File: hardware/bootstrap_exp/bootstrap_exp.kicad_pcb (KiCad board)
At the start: 4 copper layers, 45.7 x 35.6 mm, 27 parts, among them J1 Conn_Coaxial, J2 Conn_Coaxial, U1 OPA810DBV, U2 OPA810DBV, U3 OPA810DBV

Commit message: Assign names to nets
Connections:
- net Net-(R2-Pad2) renamed /BOOT_DIV
- net Net-(R4-Pad2) renamed /BOOT
- net Net-(TP5-Pad1) renamed /FRONT_OUT
- net Net-(TP6-Pad1) renamed /BOOT_BUF
- net Net-(TP7-Pad1) renamed /AMP_OUT
- net Net-(U1-Pad3) renamed /FRONT_IN
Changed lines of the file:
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@@
   (net 3 "GND")
   (net 4 "/V-")
-  (net 5 "Net-(U1-Pad3)")
+  (net 5 "/FRONT_IN")
   (net 6 "Net-(J2-Pad1)")
-  (net 7 "Net-(TP5-Pad1)")
-  (net 8 "Net-(R2-Pad2)")
-  (net 9 "Net-(R4-Pad2)")
-  (net 10 "Net-(TP6-Pad1)")
-  (net 11 "Net-(TP7-Pad1)")
+  (net 7 "/FRONT_OUT")
+  (net 8 "/BOOT_DIV")
+  (net 9 "/BOOT")
+  (net 10 "/BOOT_BUF")
+  (net 11 "/AMP_OUT")
   (footprint "Resistor_SMD:R_0603_1608Metric" (layer "F.Cu")
     (at 132.1562 100.33)
@@
     (fp_line (start -0.8 -0.4125) (end 0.8 -0.4125) (layer "F.Fab") (width 0.1))
     (pad "1" smd roundrect (at -0.825 0) (size 0.8 0.95) (layers "F.Cu" "F.Paste" "F.Mask") (roundrect_rratio 0.25)
-      (net 8 "Net-(R2-Pad2)") (pintype "passive"))
+      (net 8 "/BOOT_DIV") (pintype "passive"))
     (pad "2" smd roundrect (at 0.825 0) (size 0.8 0.95) (layers "F.Cu" "F.Paste" "F.Mask") (roundrect_rratio 0.25)
       (net 3 "GND") (pintype "passive"))
@@
     (fp_line (start -0.8 -0.4125) (end 0.8 -0.4125) (layer "F.Fab") (width 0.1))
     (pad "1" smd roundrect (at -0.825 0) (size 0.8 0.95) (layers "F.Cu" "F.Paste" "F.Mask") (roundrect_rratio 0.25)
-      (net 9 "Net-(R4-Pad2)") (pintype "passive"))
+      (net 9 "/BOOT") (pintype "passive"))
     (pad "2" smd roundrect (at 0.825 0) (size 0.8 0.95) (layers "F.Cu" "F.Paste" "F.Mask") (roundrect_rratio 0.25)
-      (net 10 "Net-(TP6-Pad1)") (pintype "passive"))
+      (net 10 "/BOOT_BUF") (pintype "passive"))
     (model "${KICAD6_3DMODEL_DIR}/Resistor_SMD.3dshapes/R_0603_1608Metric.wrl"
       (offset (xyz 0 0 0))
@@
     (fp_line (start -0.8 1.45) (end -0.8 -1.05) (layer "F.Fab") (width 0.1))
     (pad "1" smd roundrect (at -1.1375 -0.95 180) (size 1.325 0.6) (layers "F.Cu" "F.Paste" "F.Mask") (roundrect_rratio 0.25)
-      (net 10 "Net-(TP6-Pad1)") (pintype "output"))
+      (net 10 "/BOOT_BUF") (pintype "output"))
     (pad "2" smd roundrect (at -1.1375 0 180) (size 1.325 0.6) (layers "F.Cu" "F.Paste" "F.Mask") (roundrect_rratio 0.25)
       (net 4 "/V-") (pinfunction "V-") (pintype "power_in"))
     (pad "3" smd roundrect (at -1.1375 0.95 180) (size 1.325 0.6) (layers "F.Cu" "F.Paste" "F.Mask") (roundrect_rratio 0.25)
-      (net 8 "Net-(R2-Pad2)") (pinfunction "+") (pintype "input"))
+      (net 8 "/BOOT_DIV") (pinfunction "+") (pintype "input"))
     (pad "4" smd roundrect (at 1.1375 0.95 180) (size 1.325 0.6) (layers "F.Cu" "F.Paste" "F.Mask") (roundrect_rratio 0.25)
-      (net 10 "Net-(TP6-Pad1)") (pinfunction "-") (pintype "input"))
+      (net 10 "/BOOT_BUF") (pinfunction "-") (pintype "input"))
     (pad "5" smd roundrect (at 1.1375 -0.95 180) (size 1.325 0.6) (layers "F.Cu" "F.Paste" "F.Mask") (roundrect_rratio 0.25)
       (net 2 "/V+") (pinfunction "V+") (pintype "power_in"))
@@
     (fp_circle (center 0 0) (end 1.6 0) (layer "F.Fab") (width 0.15) (fill none))
     (pad "1" thru_hole circle (at 0 0) (size 2.8 2.8) (drill 1.6) (layers *.Cu *.Mask)
-      (net 11 "Net-(TP7-Pad1)") (pinfunction "1") (pintype "passive"))
+      (net 11 "/AMP_OUT") (pinfunction "1") (pintype "passive"))
     (model "${KICAD6_3DMODEL_DIR}/TestPoint.3dshapes/TestPoint_Keystone_5005-5009_Compact.wrl"
       (offset (xyz 0 0 0))
@@
     (fp_line (start 0.8 0.4125) (end -0.8 0.4125) (layer "F.Fab") (width 0.1))
     (pad "1" smd roundrect (at -0.825 0 180) (size 0.8 0.95) (layers "F.Cu" "F.Paste" "F.Mask") (roundrect_rratio 0.25)
-      (net 7 "Net-(TP5-Pad1)") (pintype "passive"))
+      (net 7 "/FRONT_OUT") (pintype "passive"))
     (pad "2" smd roundrect (at 0.825 0 180) (size 0.8 0.95) (layers "F.Cu" "F.Paste" "F.Mask") (roundrect_rratio 0.25)
-      (net 8 "Net-(R2-Pad2)") (pintype "passive"))
+      (net 8 "/BOOT_DIV") (pintype "passive"))
     (model "${KICAD6_3DMODEL_DIR}/Resistor_SMD.3dshapes/R_0603_1608Metric.wrl"
       (offset (xyz 0 0 0))
@@
     (fp_circle (center 0 0) (end 1.6 0) (layer "F.Fab") (width 0.15) (fill none))
     (pad "1" thru_hole circle (at 0 0) (size 2.8 2.8) (drill 1.6) (layers *.Cu *.Mask)
-      (net 10 "Net-(TP6-Pad1)") (pinfunction "1") (pintype "passive"))
+      (net 10 "/BOOT_BUF") (pinfunction "1") (pintype "passive"))
     (model "${KICAD6_3DMODEL_DIR}/TestPoint.3dshapes/TestPoint_Keystone_5005-5009_Compact.wrl"
       (offset (xyz 0 0 0))
@@
     (fp_line (start -0.8 -0.4125) (end 0.8 -0.4125) (layer "F.Fab") (width 0.1))
     (pad "1" smd roundrect (at -0.825 0) (size 0.8 0.95) (layers "F.Cu" "F.Paste" "F.Mask") (roundrect_rratio 0.25)
-      (net 9 "Net-(R4-Pad2)") (pintype "passive"))
+      (net 9 "/BOOT") (pintype "passive"))
     (pad "2" smd roundrect (at 0.825 0) (size 0.8 0.95) (layers "F.Cu" "F.Paste" "F.Mask") (roundrect_rratio 0.25)
-      (net 8 "Net-(R2-Pad2)") (pintype "passive"))
+      (net 8 "/BOOT_DIV") (pintype "passive"))
     (model "${KICAD6_3DMODEL_DIR}/Resistor_SMD.3dshapes/R_0603_1608Metric.wrl"
       (offset (xyz 0 0 0))
@@
     (fp_line (start -0.8 0.4125) (end -0.8 -0.4125) (layer "F.Fab") (width 0.1))
     (pad "1" smd roundrect (at -0.825 0 270) (size 0.8 0.95) (layers "F.Cu" "F.Paste" "F.Mask") (roundrect_rratio 0.25)
-      (net 5 "Net-(U1-Pad3)") (pintype "passive"))
+      (net 5 "/FRONT_IN") (pintype "passive"))
     (pad "2" smd roundrect (at 0.825 0 270) (size 0.8 0.95) (layers "F.Cu" "F.Paste" "F.Mask") (roundrect_rratio 0.25)
-      (net 9 "Net-(R4-Pad2)") (pintype "passive"))
+      (net 9 "/BOOT") (pintype "passive"))
     (model "${KICAD6_3DMODEL_DIR}/Resistor_SMD.3dshapes/R_0603_1608Metric.wrl"
       (offset (xyz 0 0 0))
@@
     (fp_circle (center 0 0) (end 1.6 0) (layer "F.Fab") (width 0.15) (fill none))
     (pad "1" thru_hole circle (at 0 0) (size 2.8 2.8) (drill 1.6) (layers *.Cu *.Mask)
-      (net 7 "Net-(TP5-Pad1)") (pinfunction "1") (pintype "passive"))
+      (net 7 "/FRONT_OUT") (pinfunction "1") (pintype "passive"))
     (model "${KICAD6_3DMODEL_DIR}/TestPoint.3dshapes/TestPoint_Keystone_5005-5009_Compact.wrl"
       (offset (xyz 0 0 0))
@@
     (fp_line (start -0.8 -0.4) (end 0.8 -0.4) (layer "F.Fab") (width 0.1))
     (pad "1" smd roundrect (at -0.775 0 180) (size 0.9 0.95) (layers "F.Cu" "F.Paste" "F.Mask") (roundrect_rratio 0.25)
-      (net 5 "Net-(U1-Pad3)") (pintype "passive"))
+      (net 5 "/FRONT_IN") (pintype "passive"))
     (pad "2" smd roundrect (at 0.775 0 180) (size 0.9 0.95) (layers "F.Cu" "F.Paste" "F.Mask") (roundrect_rratio 0.25)
       (net 1 "Net-(C1-Pad2)") (pintype "passive"))
@@
     (fp_line (start 0.8 1.45) (end -0.8 1.45) (layer "F.Fab") (width 0.1))
     (pad "1" smd roundrect (at -1.1375 -0.95) (size 1.325 0.6) (layers "F.Cu" "F.Paste" "F.Mask") (roundrect_rratio 0.25)
-      (net 7 "Net-(TP5-Pad1)") (pintype "output"))
+      (net 7 "/FRONT_OUT") (pintype "output"))
     (pad "2" smd roundrect (at -1.1375 0) (size 1.325 0.6) (layers "F.Cu" "F.Paste" "F.Mask") (roundrect_rratio 0.25)
       (net 4 "/V-") (pinfunction "V-") (pintype "power_in"))
     (pad "3" smd roundrect (at -1.1375 0.95) (size 1.325 0.6) (layers "F.Cu" "F.Paste" "F.Mask") (roundrect_rratio 0.25)
-      (net 5 "Net-(U1-Pad3)") (pinfunction "+") (pintype "input"))
+      (net 5 "/FRONT_IN") (pinfunction "+") (pintype "input"))
     (pad "4" smd roundrect (at 1.1375 0.95) (size 1.325 0.6) (layers "F.Cu" "F.Paste" "F.Mask") (roundrect_rratio 0.25)
-      (net 7 "Net-(TP5-Pad1)") (pinfunction "-") (pintype "input"))
+      (net 7 "/FRONT_OUT") (pinfunction "-") (pintype "input"))
     (pad "5" smd roundrect (at 1.1375 -0.95) (size 1.325 0.6) (layers "F.Cu" "F.Paste" "F.Mask") (roundrect_rratio 0.25)
       (net 2 "/V+") (pinfunction "V+") (pintype "power_in"))
@@
     (fp_line (start 0.8 -0.4125) (end 0.8 0.4125) (layer "F.Fab") (width 0.1))
     (pad "1" smd roundrect (at -0.825 0) (size 0.8 0.95) (layers "F.Cu" "F.Paste" "F.Mask") (roundrect_rratio 0.25)
-      (net 11 "Net-(TP7-Pad1)") (pintype "passive"))
+      (net 11 "/AMP_OUT") (pintype "passive"))
     (pad "2" smd roundrect (at 0.825 0) (size 0.8 0.95) (layers "F.Cu" "F.Paste" "F.Mask") (roundrect_rratio 0.25)
       (net 6 "Net-(J2-Pad1)") (pintype "passive"))
@@
     (fp_line (start 0.8 -1.45) (end 0.8 1.45) (layer "F.Fab") (width 0.1))
     (pad "1" smd roundrect (at -1.1375 -0.95) (size 1.325 0.6) (layers "F.Cu" "F.Paste" "F.Mask") (roundrect_rratio 0.25)
-      (net 11 "Net-(TP7-Pad1)") (pintype "output"))
+      (net 11 "/AMP_OUT") (pintype "output"))
     (pad "2" smd roundrect (at -1.1375 0) (size 1.325 0.6) (layers "F.Cu" "F.Paste" "F.Mask") (roundrect_rratio 0.25)
       (net 4 "/V-") (pinfunction "V-") (pintype "power_in"))
     (pad "3" smd roundrect (at -1.1375 0.95) (size 1.325 0.6) (layers "F.Cu" "F.Paste" "F.Mask") (roundrect_rratio 0.25)
-      (net 7 "Net-(TP5-Pad1)") (pinfunction "+") (pintype "input"))
+      (net 7 "/FRONT_OUT") (pinfunction "+") (pintype "input"))
     (pad "4" smd roundrect (at 1.1375 0.95) (size 1.325 0.6) (layers "F.Cu" "F.Paste" "F.Mask") (roundrect_rratio 0.25)
-      (net 11 "Net-(TP7-Pad1)") (pinfunction "-") (pintype "input"))
+      (net 11 "/AMP_OUT") (pinfunction "-") (pintype "input"))
     (pad "5" smd roundrect (at 1.1375 -0.95) (size 1.325 0.6) (layers "F.Cu" "F.Paste" "F.Mask") (roundrect_rratio 0.25)
       (net 2 "/V+") (pinfunction "V+") (pintype "power_in"))

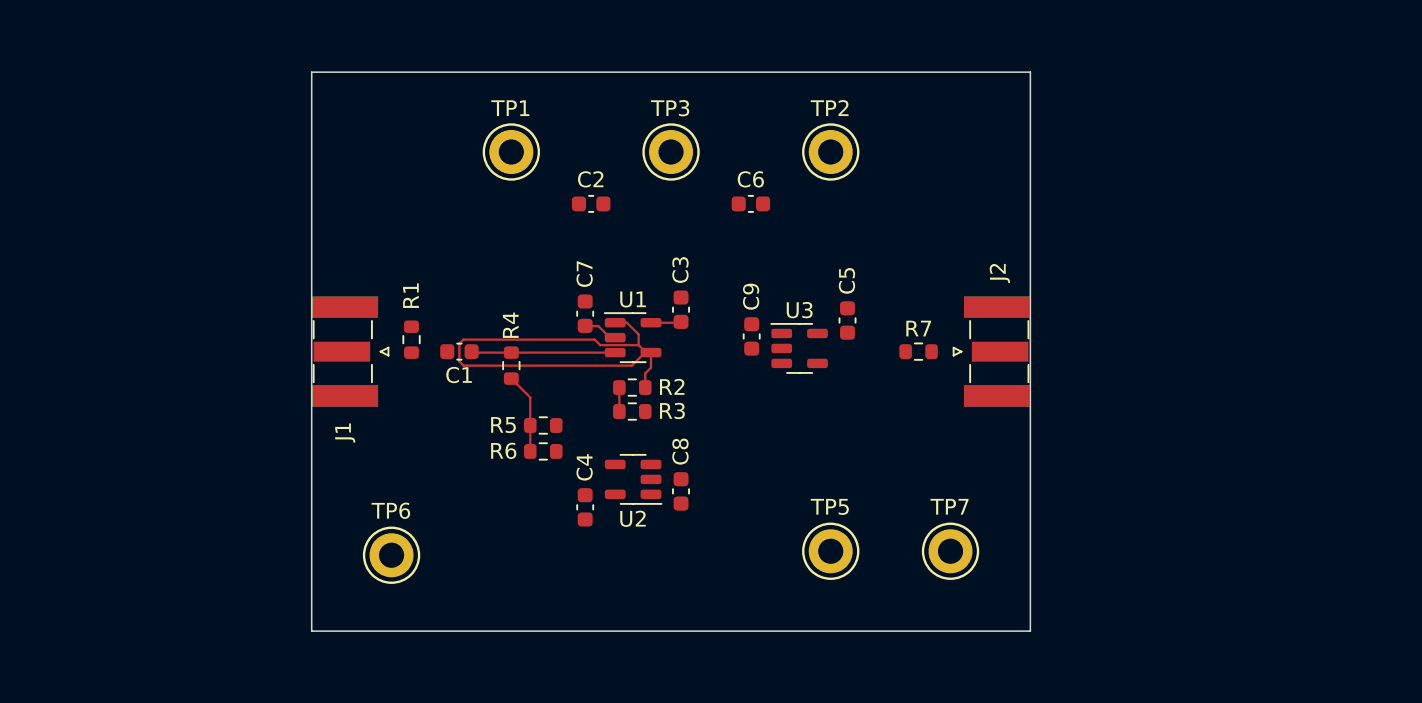
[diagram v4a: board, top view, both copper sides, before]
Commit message: Add input buffer
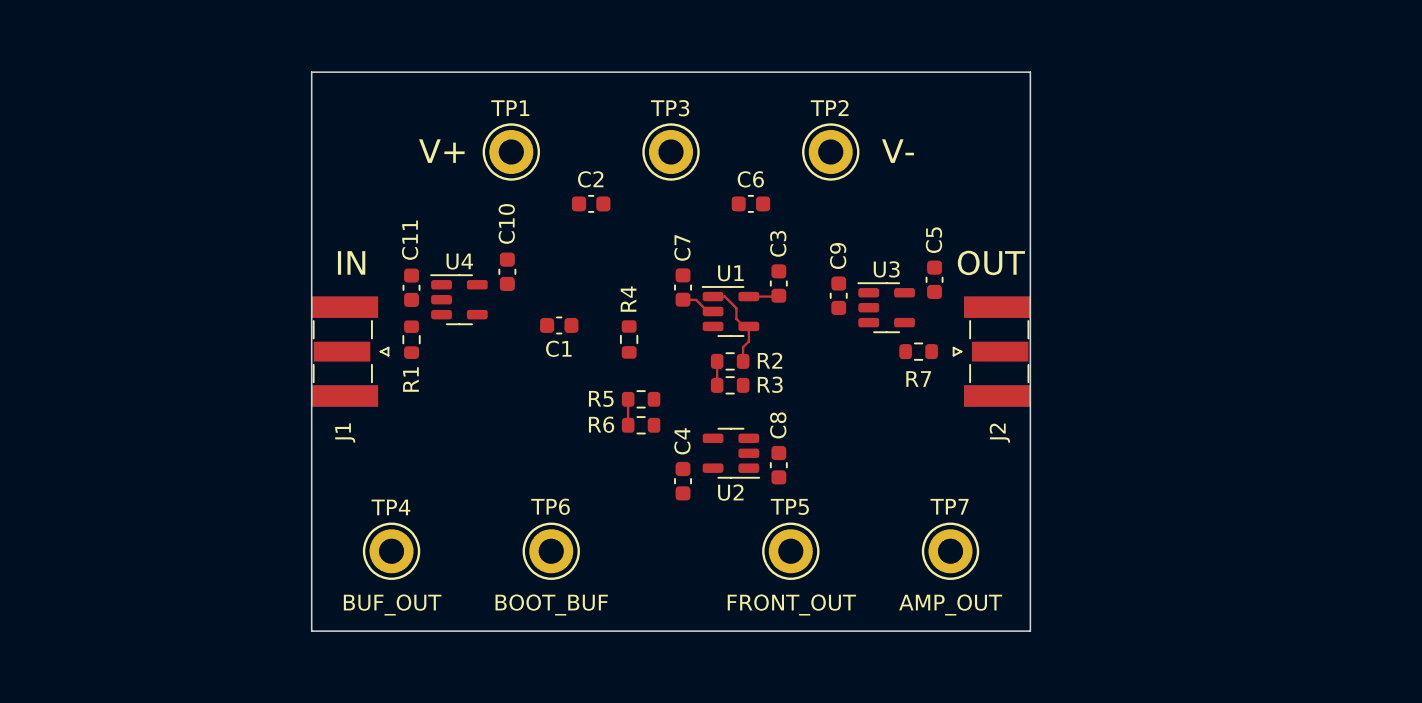
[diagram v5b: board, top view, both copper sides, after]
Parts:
- added C10: 100n, Capacitor_SMD:C_0603_1608Metric, F.Cu at (124.2, 91.4)
- added C11: 100n, Capacitor_SMD:C_0603_1608Metric, F.Cu at (118.1, 92.5)
- added TP4: ?, TestPoint:TestPoint_Keystone_5005-5009_Compact, F.Cu at (116.8, 109.2)
- added U4: OPA810DBV, Package_TO_SOT_SMD:SOT-23-5, F.Cu at (121.2, 93.2)
- moved TP6 10.2 mm to (127.0, 109.2)
- moved R4 7.68 mm to (132.0, 95.7)
- moved C1 6.56 mm to (127.5, 94.9)
- moved C3 6.44 mm to (141.5, 92.2)
- moved C4 6.44 mm to (135.4, 104.8)
- moved C7 6.44 mm to (135.4, 92.4)
- moved C8 6.44 mm to (141.5, 103.7)
- moved U1 6.44 mm to (138.4, 94.0)
- moved U2 6.44 mm to (138.4, 103.0)
- moved R6 6.44 mm to (132.7, 101.2)
- moved R5 6.44 mm to (132.7, 99.6)
- moved R2 6.44 mm to (138.4, 97.1)
- moved R3 6.44 mm to (138.4, 98.7)
- moved C9 6.11 mm to (145.3, 93.0)
- moved U3 6.11 mm to (148.3, 93.7)
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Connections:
- C1 pad 2: Net-(C1-Pad2) -> /BUF_OUT
- J1 pad 1: Net-(C1-Pad2) -> Net-(J1-Pad1)
- R1 pad 1: Net-(C1-Pad2) -> Net-(J1-Pad1)
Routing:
- net /FRONT_OUT: track 31.3 -> 5.84 mm
- net /FRONT_IN: track 9.26 -> 0.09 mm
- net /BOOT: track 5.14 -> 1.65 mm
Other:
- board text added: "AMP_OUT"
- board text added: "BOOT_BUF"
- board text added: "BUF_OUT"
- board text added: "FRONT_OUT"
- board text added: "IN"
- board text added: "OUT"
- board text added: "V+"
- board text added: "V-"

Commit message: Finish routing
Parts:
- added TP8: GND, TestPoint:TestPoint_Keystone_5005-5009_Compact, F.Cu at (134.6, 109.2)
- moved C4 2.75 mm to (135.4, 102.0), turned to 90 degrees
- moved TP6 1.27 mm to (125.7, 109.2)
- moved TP5 1.27 mm to (143.5, 109.2)
- moved C8 1.12 mm to (141.5, 102.6)
- moved U2 1.12 mm to (138.4, 101.9)
- moved R6 1.00 mm to (132.7, 100.2)
- moved R5 0.88 mm to (132.7, 98.7)
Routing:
- net /V+: track 1.93 -> 75.5 mm, vias 0 -> 4
- net /V-: track 2.22 -> 63.2 mm, vias 0 -> 4
- net GND: track 0.00 -> 28.3 mm, vias 0 -> 16
- net /BUF_OUT: track 0.00 -> 26.0 mm
- net /FRONT_OUT: track 5.84 -> 29.4 mm
- net /BOOT_BUF: track 0.00 -> 22.8 mm
- net /AMP_OUT: track 0.00 -> 19.7 mm
- net /FRONT_IN: track 0.09 -> 9.04 mm
- net Net-(J1-Pad1): track 0.00 -> 8.22 mm
- net /BOOT_DIV: track 1.52 -> 9.37 mm
- net Net-(J2-Pad1): track 0.00 -> 4.36 mm
- net /BOOT: track 1.65 -> 3.66 mm
- added copper zone on In1.Cu, net GND
- added copper zone on In2.Cu, net GND
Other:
- board text added: "GND"

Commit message: Specify dielectric for input coupling capacitance
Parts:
- C1: value 80p -> 80p/C0G
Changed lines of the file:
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@@
       (effects (font (size 1 1) (thickness 0.15)))
     )
-    (fp_text value "80p" (at 0 1.43) (layer "F.Fab")
+    (fp_text value "80p/C0G" (at 0 1.43) (layer "F.Fab")
       (effects (font (size 1 1) (thickness 0.15)))
     )

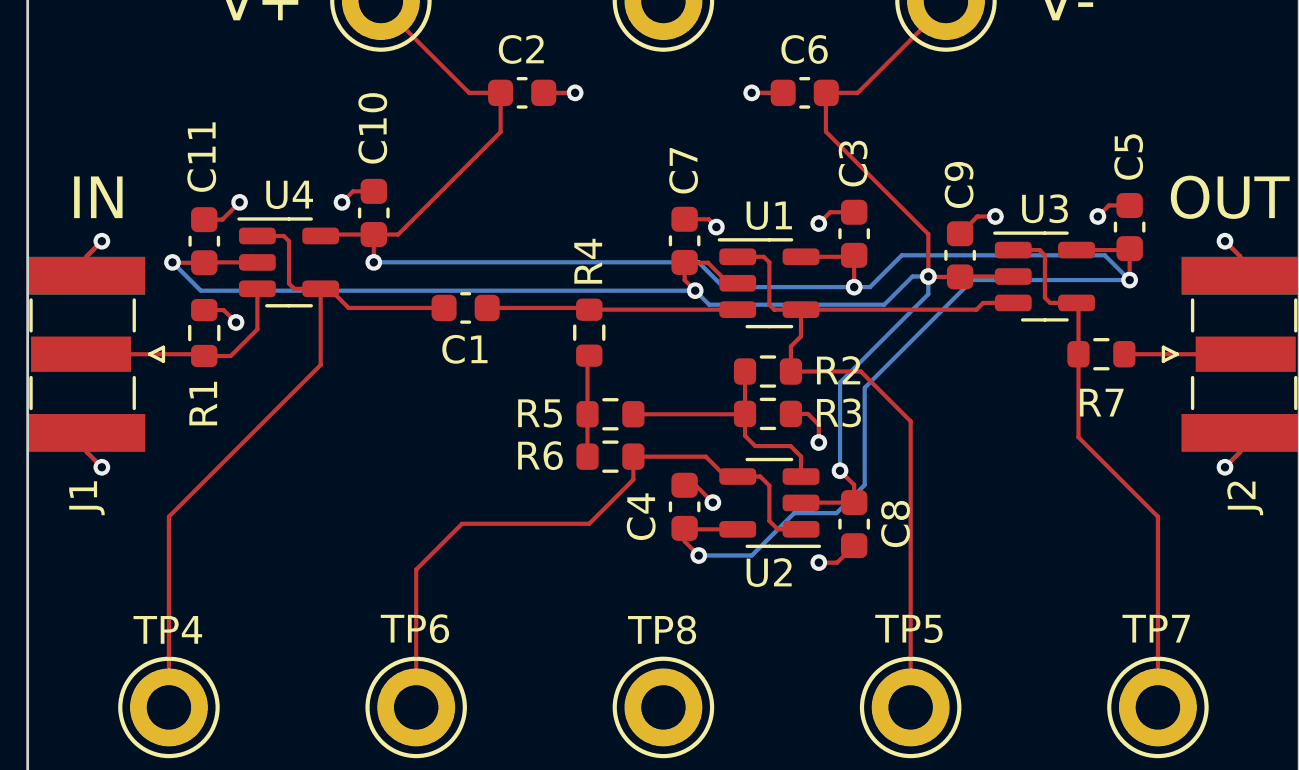
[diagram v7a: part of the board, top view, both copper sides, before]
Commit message: Reroute design for new amplifier footprint
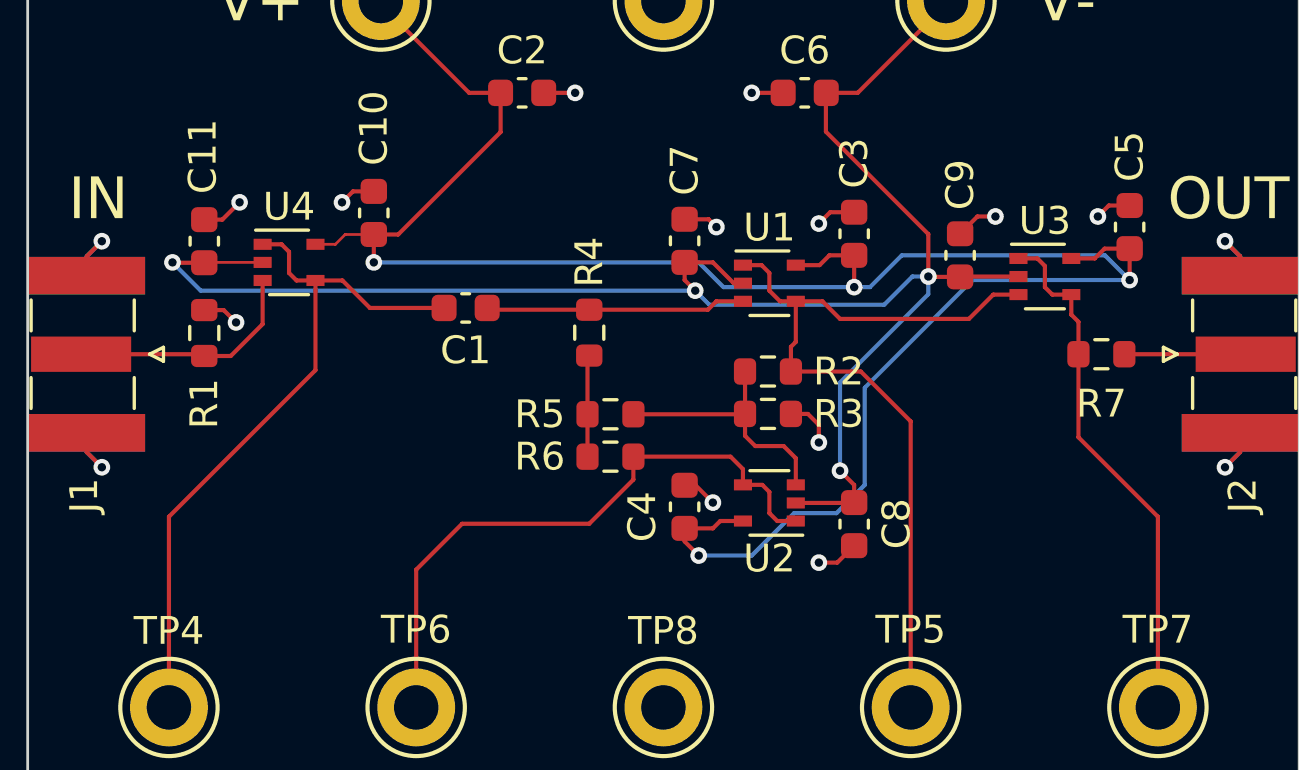
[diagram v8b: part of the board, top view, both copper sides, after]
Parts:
- U1, U2, U3, U4: footprint Package_TO_SOT_SMD:SOT-23-5 -> Package_TO_SOT_SMD:SOT-353_SC-70-5
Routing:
- net /V+: track 75.5 -> 76.7 mm
- net /V-: track 63.2 -> 64.0 mm
- net /AMP_OUT: track 19.7 -> 19.0 mm
- net /BUF_OUT: track 26.0 -> 25.5 mm
